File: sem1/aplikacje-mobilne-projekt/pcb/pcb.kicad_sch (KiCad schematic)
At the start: 5 parts

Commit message: aplikacje mobilne kicad schematic
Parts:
- added D1: DIODE, symbol pspice:DIODE
- added J1, J2: Conn_01x20_Female, symbol Connector:Conn_01x20_Female
- added M_LEFT: Motor_DC, symbol Motor:Motor_DC
- added Q1, Q10, Q11, Q12, Q2, Q3, Q4, Q9, Q?: Q_NMOS_DGS, symbol Device:Q_NMOS_DGS
- added R1: 500k, symbol Device:R
- gave numbers to parts that had none: 5
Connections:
- net +5V: now also Q6.1 (D), J1.20 (Pin_20), Q1.1 (D), Q2.1 (D), R1.1; no longer Q8.1 (D)
- net Earth: now also J2.20 (Pin_20), Q10.3 (S), Q12.3 (S), Q?.3 (S); no longer Q6.3 (S), Q7.3 (S)
- net RIGHT1: now also Q8.2 (G), J1.16 (Pin_16), Q9.2 (G); no longer Q7.2 (G)
- net RIGHT2: now also Q7.2 (G), J1.15 (Pin_15), Q10.2 (G); no longer Q8.2 (G)
- net at M_RIGHT.1 (+), Q5.3 (S): now also Q7.1 (D); no longer Q6.1 (D)
- new net: M_LEFT.1 (+), Q1.3 (S), Q3.1 (D)
- new net: Q3.3 (S), Q4.3 (S), Q7.3 (S), Q8.3 (S), Q?.1 (D)
- new net: M_RIGHT.2 (-), Q6.3 (S), Q8.1 (D)
- new net: D1.1 (K), R1.2
- new net: Q10.1 (D), Q9.3 (S)
- new net: Q11.3 (S), Q12.1 (D)
- new net: M_LEFT.2 (-), Q2.3 (S), Q4.1 (D)
- new net EMERGENCY: D1.2 (A), Q11.1 (D), Q9.1 (D), Q?.2 (G)
- new net LEFT1: J1.19 (Pin_19), Q1.2 (G), Q11.2 (G), Q4.2 (G)
- new net LEFT2: J1.18 (Pin_18), Q12.2 (G), Q2.2 (G), Q3.2 (G)
- no-connect marks 0 -> 34
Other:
- moved on the sheet: M_RIGHT, Q5, Q6, Q7, Q8

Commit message: pcb schematic update
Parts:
- added J3, J4: Conn_01x01_Female, symbol Connector:Conn_01x01_Female
- D1: value DIODE -> 1N4001; footprint (none) -> Diode_THT:D_DO-41_SOD81_P10.16mm_Horizontal; symbol pspice:DIODE -> Diode:1N4001
- Q1, Q10, Q11, Q12, Q2, Q3, Q4, Q5, Q6, Q7, Q8, Q9: value Q_NMOS_DGS -> IRL6283M; footprint (none) -> Package_DirectFET:DirectFET_MD; symbol Device:Q_NMOS_DGS -> Transistor_FET:IRL6283M
- Q13: renamed from Q?; value Q_NMOS_DGS -> IRL6283M; footprint (none) -> Package_DirectFET:DirectFET_MD; symbol Device:Q_NMOS_DGS -> Transistor_FET:IRL6283M
- renumbered M_LEFT to M_1, M_RIGHT to M_2
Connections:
- net EMERGENCY: now also D1.1 (K); no longer D1.2 (A)
- net at R1.2: now also D1.2 (A); no longer D1.1 (K)
- net +5V renamed Vcc
- net Vcc: now also J3.1 (Pin_1)
- net Earth renamed Gnd
- net Gnd: now also J4.1 (Pin_1)

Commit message: pcb
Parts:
- R1: value 500k -> 1k
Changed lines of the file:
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@@
       (effects (font (size 1.27 1.27)) (justify left))
     )
-    (property "Value" "500k" (id 1) (at 250.19 52.0699 0)
+    (property "Value" "1k" (id 1) (at 250.19 52.0699 0)
       (effects (font (size 1.27 1.27)) (justify left))
     )
@@
     )
     (path "/6121ba13-0ef7-4e06-99e1-925d76a451ab"
-      (reference "R1") (unit 1) (value "500k") (footprint "")
-    )
-  )
+      (reference "R1") (unit 1) (value "1k") (footprint "")
+    )
+  )

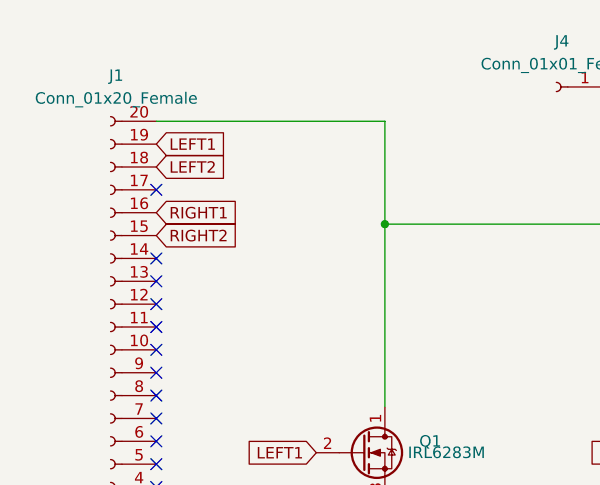
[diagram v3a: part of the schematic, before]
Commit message: apki mobilne finished software and updated kicad schematic
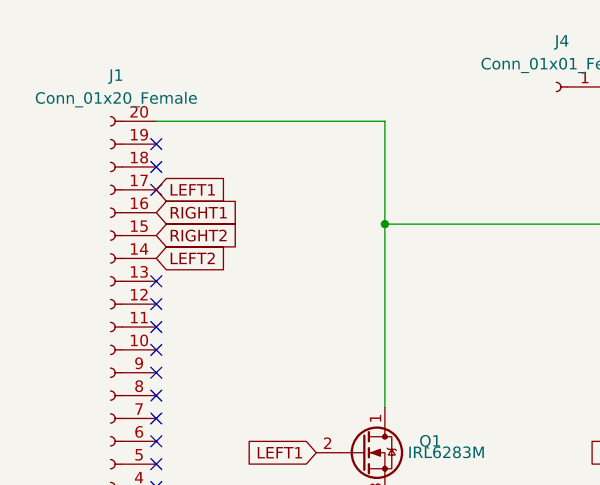
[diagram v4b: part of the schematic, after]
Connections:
- net LEFT1: now also J1.17 (Pin_17); no longer J1.19 (Pin_19)
- net LEFT2: now also J1.14 (Pin_14); no longer J1.18 (Pin_18)
- no-connect marks 34 -> 35
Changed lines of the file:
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@@
   (no_connect (at 40.64 100.33))
   (no_connect (at 40.64 50.8))
+  (no_connect (at 40.64 38.1))
   (no_connect (at 40.64 105.41))
   (no_connect (at 40.64 73.66))
+  (no_connect (at 40.64 35.56))
   (no_connect (at 40.64 110.49))
   (no_connect (at 40.64 53.34))
@@
   (no_connect (at 40.64 138.43))
   (no_connect (at 40.64 123.19))
-  (no_connect (at 40.64 48.26))
   (no_connect (at 40.64 133.35))
   (no_connect (at 40.64 60.96))
@@
     )
   )
-  (global_label "LEFT1" (shape input) (at 40.64 35.56 0) (fields_autoplaced)
-    (effects (font (size 1.27 1.27)) (justify left))
-    (property "Intersheet References" "${INTERSHEET_REFS}" (id 0) (at 48.496 35.6394 0)
-      (effects (font (size 1.27 1.27)) (justify left) hide)
-    )
-  )
   (global_label "RIGHT2" (shape input) (at 153.67 106.68 180) (fields_autoplaced)
     (effects (font (size 1.27 1.27)) (justify right))
@@
     )
   )
-  (global_label "LEFT2" (shape input) (at 40.64 38.1 0) (fields_autoplaced)
-    (effects (font (size 1.27 1.27)) (justify left))
-    (property "Intersheet References" "${INTERSHEET_REFS}" (id 0) (at 48.496 38.1794 0)
-      (effects (font (size 1.27 1.27)) (justify left) hide)
-    )
-  )
   (global_label "Vcc" (shape input) (at 137.16 44.45 90) (fields_autoplaced)
     (effects (font (size 1.27 1.27)) (justify left))
@@
     )
   )
+  (global_label "LEFT1" (shape input) (at 40.64 40.64 0) (fields_autoplaced)
+    (effects (font (size 1.27 1.27)) (justify left))
+    (property "Intersheet References" "${INTERSHEET_REFS}" (id 0) (at 48.496 40.7194 0)
+      (effects (font (size 1.27 1.27)) (justify left) hide)
+    )
+  )
   (global_label "LEFT1" (shape input) (at 58.42 69.85 180) (fields_autoplaced)
     (effects (font (size 1.27 1.27)) (justify right))
@@
     )
   )
+  (global_label "LEFT2" (shape input) (at 40.64 48.26 0) (fields_autoplaced)
+    (effects (font (size 1.27 1.27)) (justify left))
+    (property "Intersheet References" "${INTERSHEET_REFS}" (id 0) (at 48.496 48.3394 0)
+      (effects (font (size 1.27 1.27)) (justify left) hide)
+    )
+  )

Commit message: kicad schematic
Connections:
- net LEFT1: now also J1.16 (Pin_16); no longer J1.17 (Pin_17)
- net LEFT2: now also J1.17 (Pin_17); no longer J1.14 (Pin_14)
- net RIGHT1: now also J1.14 (Pin_14); no longer J1.16 (Pin_16)
- no-connect marks 35 -> 34
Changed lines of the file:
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@@
   (no_connect (at 40.64 81.28))
   (no_connect (at 40.64 140.97))
-  (no_connect (at 40.64 40.64))
   (no_connect (at 40.64 68.58))
   (no_connect (at 40.64 125.73))
@@
     (stroke (width 0) (type default) (color 0 0 0 0))
   )
-  (global_label "RIGHT1" (shape input) (at 40.64 43.18 0) (fields_autoplaced)
-    (effects (font (size 1.27 1.27)) (justify left))
-    (property "Intersheet References" "${INTERSHEET_REFS}" (id 0) (at 49.7055 43.1006 0)
-      (effects (font (size 1.27 1.27)) (justify left) hide)
-    )
-  )
   (global_label "RIGHT1" (shape input) (at 191.77 107.95 180) (fields_autoplaced)
     (effects (font (size 1.27 1.27)) (justify right))
@@
     )
   )
+  (global_label "LEFT1" (shape input) (at 40.64 43.18 0) (fields_autoplaced)
+    (effects (font (size 1.27 1.27)) (justify left))
+    (property "Intersheet References" "${INTERSHEET_REFS}" (id 0) (at 48.496 43.2594 0)
+      (effects (font (size 1.27 1.27)) (justify left) hide)
+    )
+  )
   (global_label "Gnd" (shape input) (at 247.65 113.03 270) (fields_autoplaced)
     (effects (font (size 1.27 1.27)) (justify right))
@@
     )
   )
+  (global_label "LEFT2" (shape input) (at 40.64 40.64 0) (fields_autoplaced)
+    (effects (font (size 1.27 1.27)) (justify left))
+    (property "Intersheet References" "${INTERSHEET_REFS}" (id 0) (at 48.496 40.7194 0)
+      (effects (font (size 1.27 1.27)) (justify left) hide)
+    )
+  )
   (global_label "RIGHT2" (shape input) (at 40.64 45.72 0) (fields_autoplaced)
     (effects (font (size 1.27 1.27)) (justify left))
@@
     )
   )
-  (global_label "LEFT1" (shape input) (at 40.64 40.64 0) (fields_autoplaced)
-    (effects (font (size 1.27 1.27)) (justify left))
-    (property "Intersheet References" "${INTERSHEET_REFS}" (id 0) (at 48.496 40.7194 0)
+  (global_label "RIGHT1" (shape input) (at 40.64 48.26 0) (fields_autoplaced)
+    (effects (font (size 1.27 1.27)) (justify left))
+    (property "Intersheet References" "${INTERSHEET_REFS}" (id 0) (at 49.7055 48.1806 0)
       (effects (font (size 1.27 1.27)) (justify left) hide)
     )
@@
     )
   )
-  (global_label "LEFT2" (shape input) (at 40.64 48.26 0) (fields_autoplaced)
-    (effects (font (size 1.27 1.27)) (justify left))
-    (property "Intersheet References" "${INTERSHEET_REFS}" (id 0) (at 48.496 48.3394 0)
-      (effects (font (size 1.27 1.27)) (justify left) hide)
-    )
-  )

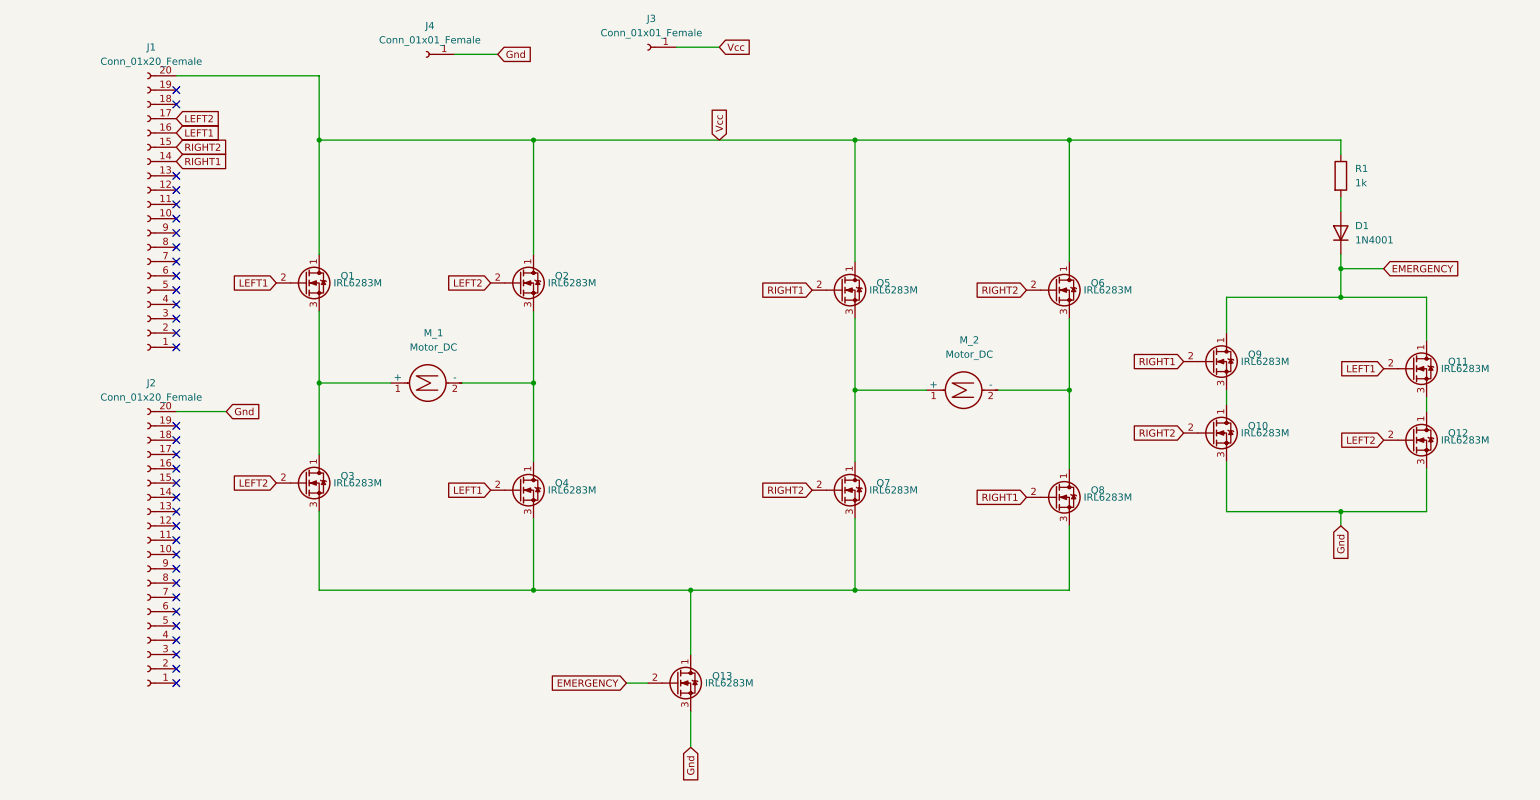
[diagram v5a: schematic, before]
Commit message: update aplikacje mobilne schematic
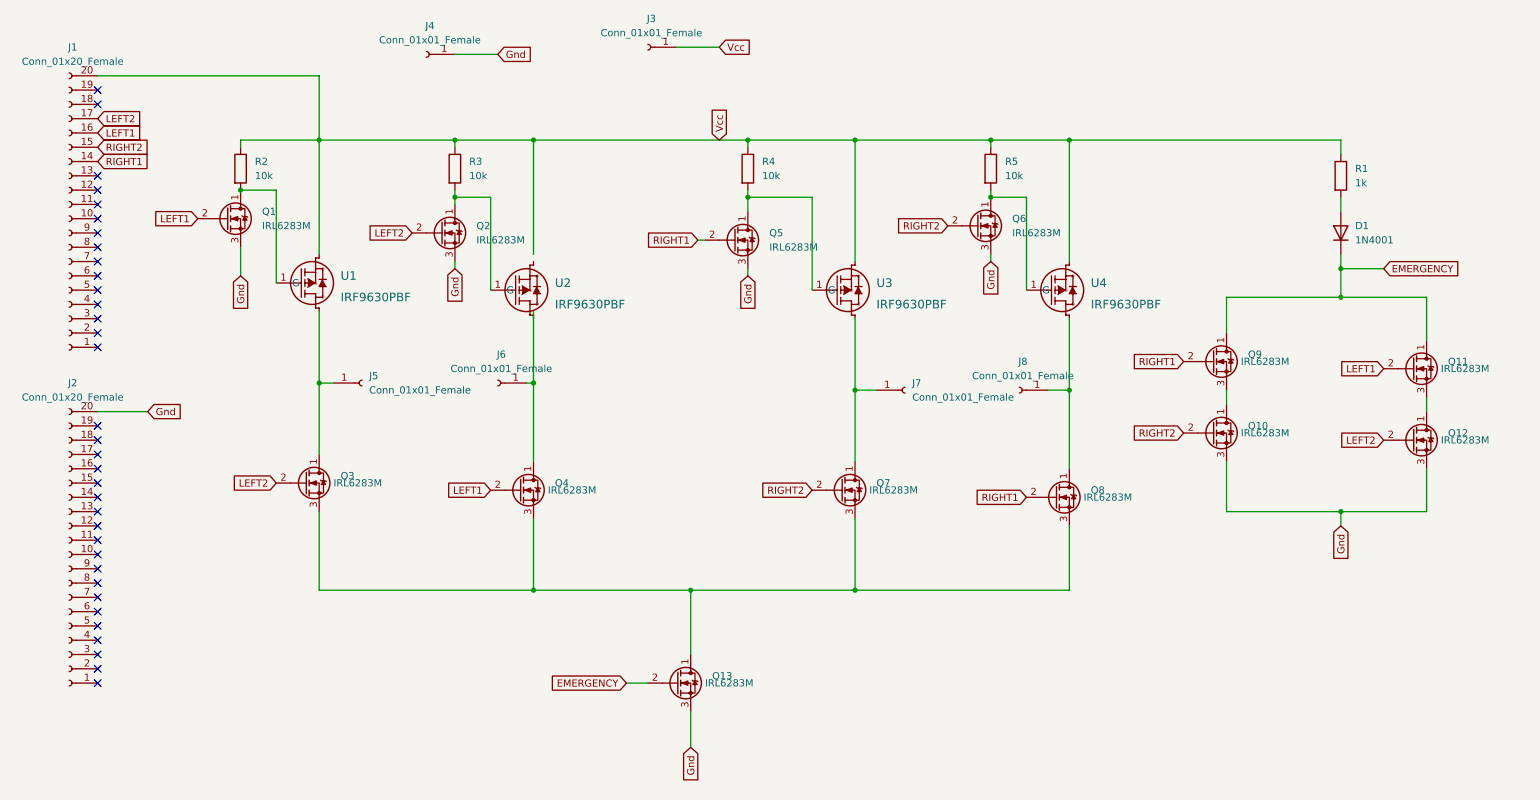
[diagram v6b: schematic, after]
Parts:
- removed M_1, M_2: Motor_DC, symbol Motor:Motor_DC
- added J5, J6, J7, J8: Conn_01x01_Female, symbol Connector:Conn_01x01_Female
- added R2, R3, R4, R5: 10k, symbol Device:R
- added U1, U2, U3, U4: IRF9630PBF, TO220AB_VIS, symbol 2025-01-16_19-49-32:IRF9630PBF
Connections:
- net Gnd: now also Q1.3 (S), Q2.3 (S), Q5.3 (S), Q6.3 (S)
- net Vcc: now also R2.1, R3.1, R4.1, R5.1; no longer Q1.1 (D), Q2.1 (D), Q5.1 (D), Q6.1 (D)
- net at Q3.1 (D): now also J5.1 (Pin_1); no longer Q1.3 (S)
- net at Q7.1 (D): now also J7.1 (Pin_1); no longer Q5.3 (S)
- net at Q8.1 (D): now also J8.1 (Pin_1); no longer Q6.3 (S)
- net at Q4.1 (D): now also J6.1 (Pin_1); no longer Q2.3 (S)
- new net: Q1.1 (D), R2.2, U1.1 (G)
- new net: Q6.1 (D), R5.2, U4.1 (G)
- new net: Q5.1 (D), R4.2, U3.1 (G)
- new net: Q2.1 (D), R3.2, U2.1 (G)
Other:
- moved on the sheet: J1, J2
